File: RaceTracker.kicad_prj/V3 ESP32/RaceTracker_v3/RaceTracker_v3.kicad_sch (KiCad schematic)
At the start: 39 parts, among them J1 USB-C, J2 Battery, J3 Qwiic GPS (I2C), J4 microSD, J5 UART Debug, SW1 PWR, SW2 RESET, SW3 BOOT, U1 ESP32-S3-WROOM-1-N8, U2 MCP73831T-2ACI/OT, U3 AP2112K-3.3

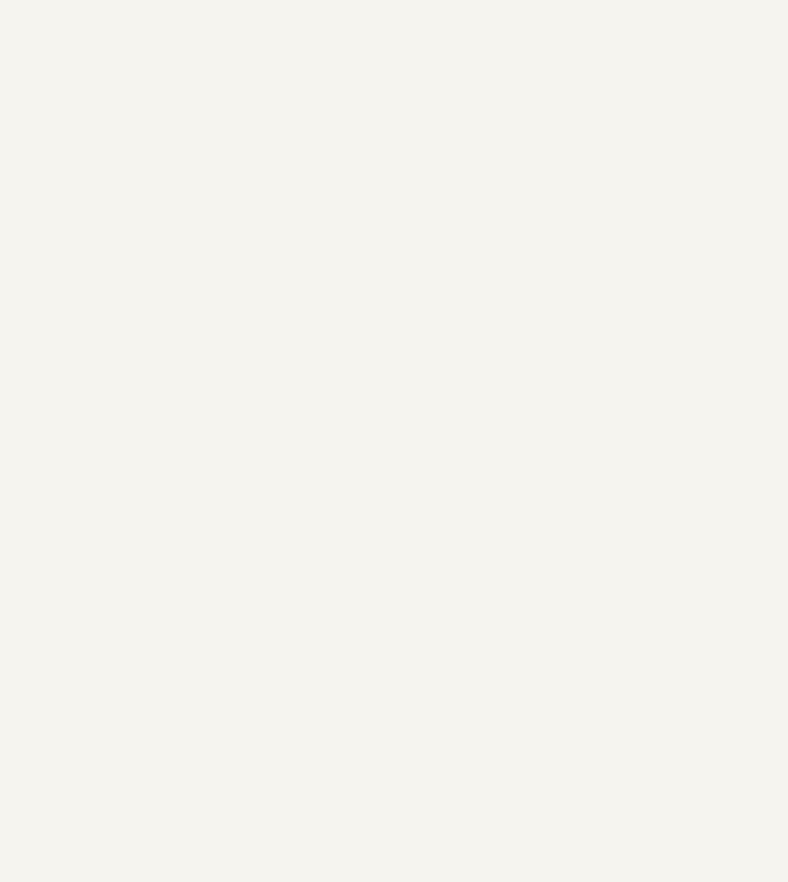
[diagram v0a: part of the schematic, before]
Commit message: V3: Wuerth WSEN-ISDS (2536030320001) 6-Achsen-IMU ergaenzt
Beschaltung exakt nach Datenblatt (Rev 001.005, 2025-10-30):
- VDD + VDD_IO an +3V3, je 100nF Entkopplung (C11/C12) -- Standard-
  Bypass-Praxis, da dieses Datenblatt (anders als ESP32/MCP73831/
  AP2112K) keine eigene Beispielschaltung zeigt.
- Pin 2/3 (RSVD) zwingend an VDD_IO (Datenblatt: "Optimize power
  consumption during device start-up sequence").
- Pin 11 (RSVD) an VDD_IO (Datenblatt bietet Wahl: VDD_IO oder NC).
- Pin 10 (RSVD) explizit unverbunden (Datenblatt: "Leave electrically
  unconnected and solder to the PCB").
- CS an VDD_IO (aktiviert I2C-Modus statt SPI).
- SAO ueber R15 (10k) nach GND (I2C-Adresse) -- Pull-Widerstand statt
  Direktverbindung, passend zum Board-Konvention (R1-R14 sind alle
  Pull-Widerstaende) und vermeidet eine ERC-Warnung (Bidirectional-Pin
  direkt an denselben Netz-Knoten wie der GND-PWR_FLAG).
- SCL/SDA an den bestehenden I2C-Bus (teilt sich mit dem externen
  GPS-Modul an J3).
- INT_0/INT_1 offen (optionale Wake/Data-Ready-Ausgaenge, fuer reines
  I2C-Polling nicht noetig) -- explizite No-Connect-Marker.

Kein offizielles KiCad-Symbol fuer dieses Bauteil vorhanden -- eigenes
14-Pin-Symbol gezeichnet, echtes Footprint "Package_LGA:LGA-14_3x2.5mm_
P0.5mm_LayoutBorder3x4y" (urspruenglich fuer ST LSM6DS3 erstellt --
identisches LGA-14/0.5mm-Pitch/3-4-3-4-Pinout-Package, Land-Pattern-Maße
im WSEN-ISDS-Datenblatt gegengeprueft). Neue projektlokale Symbolbib-
liothek RaceTracker_v3.kicad_sym + sym-lib-table angelegt (vermeidet
die lib_symbol_issues-Warnung).

Platine von 50x73mm auf 50x85mm vergroessert (war bereits komplett
vollgepackt, kein Platz fuer 4 neue Bauteile) -- neue Reihe U4/R15/C11/
C12 unten platziert, bestehende Platzierung unangetastet. Default-
Clearance von 0.2mm auf 0.127mm gelockert (die LGA-14-eigenen Pads
liegen bauartbedingt bei 0.5mm Pitch teils nur 0.15-0.175mm auseinander
-- selbe Art Fix wie zuvor bei den ESP32-EPAD-Vias).

ERC: 0 Fehler, 0 Warn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
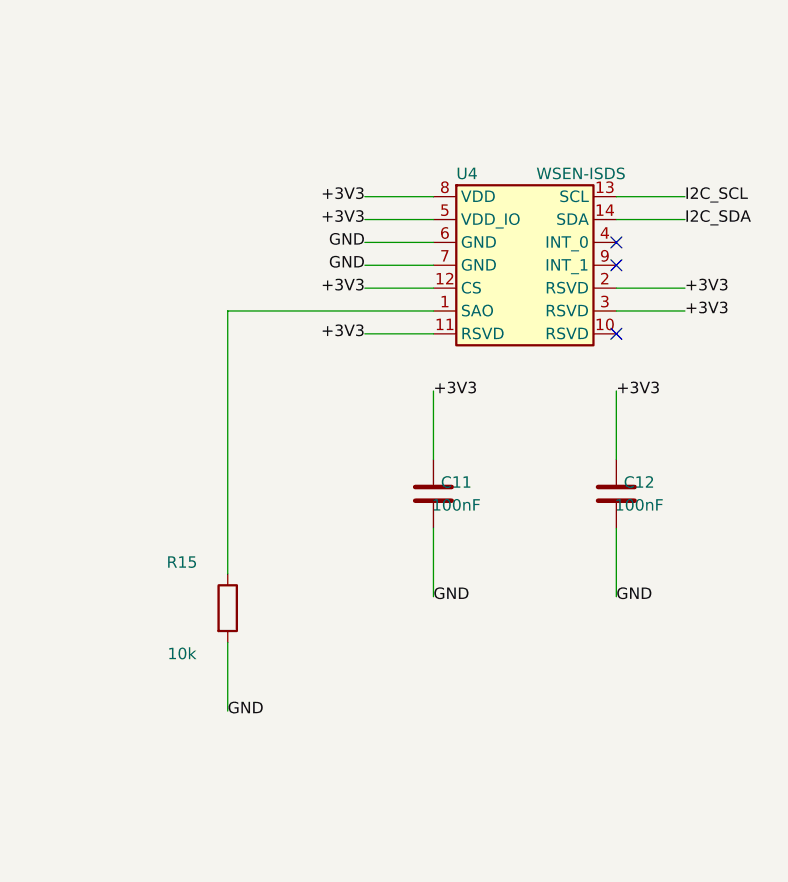
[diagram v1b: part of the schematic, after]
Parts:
- added C11, C12: 100nF, Capacitor_SMD:C_0603_1608Metric, symbol Device:C
- added R15: 10k, Resistor_SMD:R_0603_1608Metric, symbol Device:R
- added U4: WSEN-ISDS, Package_LGA:LGA-14_3x2.5mm_P0.5mm_LayoutBorder3x4y, symbol RaceTracker_v3:WSEN-ISDS
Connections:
- net +3V3: now also C11.1, C12.1, U4.11 (RSVD), U4.12 (CS), U4.2 (RSVD), U4.3 (RSVD), U4.5 (VDD_IO), U4.8 (VDD)
- net GND: now also C11.2, C12.2, R15.2, U4.6 (GND), U4.7 (GND)
- net I2C_SCL: now also U4.13 (SCL)
- net I2C_SDA: now also U4.14 (SDA)
- new net: R15.1, U4.1 (SAO)
- no-connect marks 28 -> 31

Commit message: V3: PCB auf 4 Lagen (JLCPCB-Standard-Stackup) + C13 (10uF) fuer WSEN-ISDS
Layer-Stackup 2 -> 4 Lagen (In1.Cu/In2.Cu ergaenzt), physischer Aufbau
exakt nach JLCPCB-Standard-4-Lagen-1.6mm-Build (JLC7628-Klasse):
F.Cu 1oz / Prepreg 7628 0.2104mm / In1.Cu 0.5oz / Core FR4 1.065mm /
In2.Cu 0.5oz / Prepreg 7628 0.2104mm / B.Cu 1oz -- angelegt fuer GND-
und VCC-Plane auf den Innenlagen (Zonen/Pours folgen beim eigentlichen
Routing).

C13 (10uF, 0805) ergaenzt: erneute Pruefung von Wuerths eigenem
"Application circuit" (User Manual Figur 3, Seite 17) zeigte, dass VDD
zusaetzlich zum 100nF (C11) auch einen 10uF-Bulk-Kondensator parallel
braucht ("highly recommended") -- war in der ersten Bestueckung uebersehen
worden. VDD_IO (C12, nur 100nF) stimmte bereits exakt mit der Abbildung
ueberein. User-Manual als Referenz mit im Projekt abgelegt.

ERC: 0/0. DRC: 0 Violations, 122 unverbundene Punkte (weiterhin
ungeroutet, erwartet).

Co-Authored-By: Claude Sonnet 5 <noreply@anthropic.com>
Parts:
- added C13: 10uF, Capacitor_SMD:C_0805_2012Metric, symbol Device:C
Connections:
- net +3V3: now also C13.1
- net GND: now also C13.2
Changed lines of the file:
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@@
+		)
+	)
+	(symbol
+		(lib_id "Device:C")
+		(at 462.28 127.0 0)
+		(unit 1)
+		(body_style 1)
+		(exclude_from_sim no)
+		(in_bom yes)
+		(on_board yes)
+		(in_pos_files yes)
+		(dnp no)
+		(property "Reference" "C13"
+			(at 464.82 125.73 0)
+			(show_name no)
+			(do_not_autoplace no)
+			(effects
+				(font
+					(size 1.27 1.27)
+				)
+			)
+		)
+		(property "Value" "10uF"
+			(at 464.82 128.27 0)
+			(show_name no)
+			(do_not_autoplace no)
+			(effects
+				(font
+					(size 1.27 1.27)
+				)
+			)
+		)
+		(property "Footprint" "Capacitor_SMD:C_0805_2012Metric"
+			(at 462.28 127.0 0)
+			(hide yes)
+			(show_name no)
+			(do_not_autoplace no)
+			(effects
+				(font
+					(size 1.27 1.27)
+				)
+			)
+		)
+		(property "Datasheet" ""
+			(at 462.28 127.0 0)
+			(hide yes)
+			(show_name no)
+			(do_not_autoplace no)
+			(effects
+				(font
+					(size 1.27 1.27)
+				)
+			)
+		)
+		(property "Description" ""
+			(at 462.28 127.0 0)
+			(show_name no)
+			(do_not_autoplace no)
+			(effects
+				(font
+					(size 1.27 1.27)
+				)
+			)
+		)
+		(pin "1"
+		)
+		(pin "2"
+		)
+		(instances
+			(project "RaceTracker_v3"
+				(path "/4ed299f8-94b7-4355-9e61-0164201a9634"
+					(reference "C13")
+					(unit 1)
+				)
+			)
+		)
+	)
+	(wire
+		(pts
+			(xy 462.28 123.19) (xy 462.28 115.57)
+		)
+		(stroke
+			(width 0)
+			(type default)
+		)
+	)
+	(label "+3V3"
+		(at 462.28 115.57 0)
+		(effects
+			(font
+				(size 1.27 1.27)
+			)
+			(justify left)
+		)
+	)
+	(wire
+		(pts
+			(xy 462.28 130.81) (xy 462.28 138.43)
+		)
+		(stroke
+			(width 0)
+			(type default)
+		)
+	)
+	(label "GND"
+		(at 462.28 138.43 0)
+		(effects
+			(font
+				(size 1.27 1.27)
+			)
+			(justify left)
 		)
 	)
